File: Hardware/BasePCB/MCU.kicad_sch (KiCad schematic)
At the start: 24 parts, among them J7 Conn_01x04, Q10 IRLML0030, Q11 IRLML0030, U5 LeaderSOM

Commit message: only 4 traces left
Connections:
- net SuppReg_ADC: now also R9.1; no longer R40.1
- net SuppReg_ADC_filtered: now also C14.1, R9.2, U5.39 (ADC1_IN3); no longer C13.1, R40.2, U5.33 (ADC1_IN15)
- net SuppReg_I_ADC: now also R35.1; no longer R9.1
- net SuppReg_I_ADC_filtered: now also C11.1, R35.2, U5.31 (ADC1_IN12); no longer C14.1, R9.2, U5.39 (ADC1_IN3)
- net Supp_ADC: now also R45.1; no longer R35.1
- net Supp_ADC_filtered: now also C15.1, R45.2, U5.41 (ADC1_IN2); no longer C11.1, R35.2, U5.31 (ADC1_IN12)
- net Supp_I_ADC: now also R40.1; no longer R45.1
- net Supp_I_ADC_filtered: now also C13.1, R40.2, U5.33 (ADC1_IN15); no longer C15.1, R45.2, U5.41 (ADC1_IN2)
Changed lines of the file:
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@@
 	)
 	(junction
-		(at 52.07 104.14)
+		(at 121.92 72.39)
 		(diameter 0)
 		(color 0 0 0 0)
 	)
 	(junction
-		(at 121.92 72.39)
+		(at 121.92 74.93)
 		(diameter 0)
 		(color 0 0 0 0)
 	)
 	(junction
-		(at 107.95 104.14)
+		(at 34.29 26.67)
 		(diameter 0)
 		(color 0 0 0 0)
 	)
 	(junction
-		(at 121.92 74.93)
+		(at 121.92 64.77)
 		(diameter 0)
 		(color 0 0 0 0)
 	)
 	(junction
-		(at 34.29 26.67)
+		(at 107.95 128.27)
 		(diameter 0)
 		(color 0 0 0 0)
 	)
 	(junction
-		(at 121.92 64.77)
+		(at 52.07 129.54)
 		(diameter 0)
 		(color 0 0 0 0)
@@
 	)
 	(junction
-		(at 107.95 128.27)
+		(at 252.73 58.42)
 		(diameter 0)
 		(color 0 0 0 0)
 	)
 	(junction
-		(at 52.07 129.54)
+		(at 121.92 69.85)
 		(diameter 0)
 		(color 0 0 0 0)
 	)
 	(junction
-		(at 252.73 58.42)
+		(at 52.07 104.14)
 		(diameter 0)
 		(color 0 0 0 0)
 	)
 	(junction
-		(at 121.92 69.85)
+		(at 121.92 67.31)
 		(diameter 0)
 		(color 0 0 0 0)
 	)
 	(junction
-		(at 121.92 67.31)
+		(at 107.95 104.14)
 		(diameter 0)
 		(color 0 0 0 0)
@@
 	(wire
 		(pts
+			(xy 165.1 38.1) (xy 190.5 38.1)
+		)
+		(stroke
+			(width 0)
+			(type default)
+		)
+	)
+	(wire
+		(pts
 			(xy 252.73 30.48) (xy 255.27 30.48)
 		)
@@
 	(wire
 		(pts
+			(xy 39.37 129.54) (xy 41.91 129.54)
+		)
+		(stroke
+			(width 0)
+			(type default)
+		)
+	)
+	(wire
+		(pts
 			(xy 40.64 54.61) (xy 45.72 54.61)
 		)
@@
 	(wire
 		(pts
-			(xy 43.18 33.02) (xy 43.18 35.56)
+			(xy 52.07 129.54) (xy 73.66 129.54)
 		)
 		(stroke
@@
 	(wire
 		(pts
-			(xy 43.18 40.64) (xy 45.72 40.64)
+			(xy 43.18 33.02) (xy 43.18 35.56)
 		)
 		(stroke
@@
 	(wire
 		(pts
-			(xy 252.73 35.56) (xy 255.27 35.56)
+			(xy 43.18 40.64) (xy 45.72 40.64)
 		)
 		(stroke
@@
 	(wire
 		(pts
-			(xy 191.77 113.03) (xy 191.77 115.57)
+			(xy 252.73 35.56) (xy 255.27 35.56)
 		)
 		(stroke
@@
 	(wire
 		(pts
-			(xy 36.83 104.14) (xy 41.91 104.14)
+			(xy 191.77 113.03) (xy 191.77 115.57)
 		)
 		(stroke
@@
 	(wire
 		(pts
-			(xy 40.64 57.15) (xy 45.72 57.15)
+			(xy 52.07 104.14) (xy 74.93 104.14)
 		)
 		(stroke
@@
 	(wire
 		(pts
-			(xy 218.44 30.48) (xy 218.44 31.75)
+			(xy 40.64 57.15) (xy 45.72 57.15)
 		)
 		(stroke
@@
 	(wire
 		(pts
-			(xy 92.71 68.58) (xy 83.82 68.58)
+			(xy 218.44 30.48) (xy 218.44 31.75)
 		)
 		(stroke
@@
 	(wire
 		(pts
-			(xy 43.18 35.56) (xy 43.18 38.1)
+			(xy 92.71 68.58) (xy 83.82 68.58)
 		)
 		(stroke
@@
 	(wire
 		(pts
-			(xy 43.18 38.1) (xy 43.18 40.64)
+			(xy 43.18 35.56) (xy 43.18 38.1)
 		)
 		(stroke
@@
 	(wire
 		(pts
-			(xy 107.95 111.76) (xy 107.95 114.3)
+			(xy 43.18 38.1) (xy 43.18 40.64)
 		)
 		(stroke
@@
 	(wire
 		(pts
-			(xy 165.1 38.1) (xy 190.5 38.1)
+			(xy 107.95 111.76) (xy 107.95 114.3)
 		)
 		(stroke
@@
 	(wire
 		(pts
-			(xy 191.77 101.6) (xy 191.77 105.41)
+			(xy 107.95 104.14) (xy 130.81 104.14)
 		)
 		(stroke
@@
 	(wire
 		(pts
-			(xy 38.1 129.54) (xy 41.91 129.54)
+			(xy 191.77 101.6) (xy 191.77 105.41)
 		)
 		(stroke
@@
 	(wire
 		(pts
-			(xy 165.1 30.48) (xy 190.5 30.48)
+			(xy 83.82 53.34) (xy 96.52 53.34)
 		)
 		(stroke
@@
 	(wire
 		(pts
-			(xy 83.82 53.34) (xy 96.52 53.34)
+			(xy 191.77 115.57) (xy 195.58 115.57)
 		)
 		(stroke
@@
 	(wire
 		(pts
-			(xy 191.77 115.57) (xy 195.58 115.57)
+			(xy 93.98 104.14) (xy 97.79 104.14)
+		)
+		(stroke
+			(width 0)
+			(type default)
+		)
+	)
+	(wire
+		(pts
+			(xy 38.1 104.14) (xy 41.91 104.14)
 		)
 		(stroke
@@
 	(wire
 		(pts
-			(xy 118.11 38.1) (xy 127 38.1)
+			(xy 107.95 128.27) (xy 127 128.27)
 		)
 		(stroke
@@
 	(wire
 		(pts
-			(xy 107.95 104.14) (xy 127 104.14)
+			(xy 118.11 38.1) (xy 127 38.1)
 		)
 		(stroke
@@
 	(wire
 		(pts
-			(xy 52.07 129.54) (xy 74.93 129.54)
+			(xy 165.1 30.48) (xy 190.5 30.48)
 		)
 		(stroke
@@
 	(wire
 		(pts
+			(xy 93.98 128.27) (xy 97.79 128.27)
+		)
+		(stroke
+			(width 0)
+			(type default)
+		)
+	)
+	(wire
+		(pts
 			(xy 218.44 100.33) (xy 218.44 101.6)
 		)
@@
 	(wire
 		(pts
-			(xy 93.98 104.14) (xy 97.79 104.14)
+			(xy 165.1 71.12) (xy 186.69 71.12)
 		)
 		(stroke
@@
 	(wire
 		(pts
-			(xy 165.1 71.12) (xy 186.69 71.12)
+			(xy 242.57 69.85) (xy 259.08 69.85)
 		)
 		(stroke
@@
 	(wire
 		(pts
-			(xy 242.57 69.85) (xy 259.08 69.85)
+			(xy 165.1 33.02) (xy 190.5 33.02)
 		)
 		(stroke
@@
 	(wire
 		(pts
-			(xy 148.59 115.57) (xy 152.4 115.57)
+			(xy 165.1 43.18) (xy 190.5 43.18)
 		)
 		(stroke
@@
 	(wire
 		(pts
-			(xy 83.82 60.96) (xy 92.71 60.96)
+			(xy 148.59 115.57) (xy 152.4 115.57)
 		)
 		(stroke
@@
 	(wire
 		(pts
-			(xy 34.29 35.56) (xy 34.29 38.1)
+			(xy 83.82 60.96) (xy 92.71 60.96)
 		)
 		(stroke
@@
 	(wire
 		(pts
-			(xy 92.71 66.04) (xy 83.82 66.04)
+			(xy 34.29 35.56) (xy 34.29 38.1)
 		)
 		(stroke
@@
 	(wire
 		(pts
-			(xy 165.1 68.58) (xy 186.69 68.58)
+			(xy 92.71 66.04) (xy 83.82 66.04)
 		)
 		(stroke
@@
 	(wire
 		(pts
-			(xy 248.92 58.42) (xy 252.73 58.42)
+			(xy 165.1 68.58) (xy 186.69 68.58)
 		)
 		(stroke
@@
 	(wire
 		(pts
-			(xy 107.95 128.27) (xy 130.81 128.27)
+			(xy 248.92 58.42) (xy 252.73 58.42)
 		)
 		(stroke
@@
 	(wire
 		(pts
-			(xy 165.1 43.18) (xy 190.5 43.18)
-		)
-		(stroke
-			(width 0)
-			(type default)
-		)
-	)
-	(wire
-		(pts
-			(xy 93.98 128.27) (xy 97.79 128.27)
-		)
-		(stroke
-			(width 0)
-			(type default)
-		)
-	)
-	(wire
-		(pts
 			(xy 160.02 120.65) (xy 160.02 127)
 		)
@@
 		)
 	)
-	(wire
-		(pts
-			(xy 165.1 33.02) (xy 190.5 33.02)
-		)
-		(stroke
-			(width 0)
-			(type default)
-		)
-	)
 	(bus
 		(pts
@@
 	(wire
 		(pts
-			(xy 52.07 104.14) (xy 71.12 104.14)
-		)
-		(stroke
-			(width 0)
-			(type default)
-		)
-	)
-	(wire
-		(pts
 			(xy 52.07 111.76) (xy 52.07 114.3)
 		)
@@
 	)
 	(label "SuppReg_ADC_filtered"
-		(at 127 104.14 180)
+		(at 73.66 129.54 180)
 		(effects
 			(font
@@
 	)
 	(label "Supp_I_ADC_filtered"
-		(at 130.81 128.27 180)
+		(at 130.81 104.14 180)
 		(effects
 			(font
@@
 	)
 	(label "Supp_ADC_filtered"
-		(at 71.12 104.14 180)
+		(at 127 128.27 180)
 		(effects
 			(font
@@
 	)
 	(label "SuppReg_ADC_filtered"
-		(at 190.5 33.02 180)
+		(at 190.5 38.1 180)
 		(effects
 			(font
@@
 	)
 	(label "Supp_ADC_filtered"
-		(at 190.5 30.48 180)
+		(at 190.5 43.18 180)
 		(effects
 			(font
@@
 	)
 	(label "SuppReg_I_ADC_filtered"
-		(at 74.93 129.54 180)
+		(at 74.93 104.14 180)
 		(effects
 			(font
@@
 	)
 	(label "SuppReg_I_ADC_filtered"
-		(at 190.5 38.1 180)
+		(at 190.5 30.48 180)
 		(effects
 			(font
@@
 	)
 	(label "Supp_I_ADC_filtered"
-		(at 190.5 43.18 180)
+		(at 190.5 33.02 180)
 		(effects
 			(font
@@
 	(hierarchical_label "SuppReg_ADC"
 		(shape input)
-		(at 93.98 104.14 180)
+		(at 39.37 129.54 180)
 		(effects
 			(font
@@
 	(hierarchical_label "SuppReg_I_ADC"
 		(shape input)
-		(at 38.1 129.54 180)
+		(at 38.1 104.14 180)
 		(effects
 			(font
@@
 	(hierarchical_label "Supp_I_ADC"
 		(shape input)
-		(at 93.98 128.27 180)
+		(at 93.98 104.14 180)
 		(effects
 			(font
@@
 	(hierarchical_label "Supp_ADC"
 		(shape input)
-		(at 36.83 104.14 180)
+		(at 93.98 128.27 180)
 		(effects
 			(font

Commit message: align things
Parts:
- added D6: LED, LED_SMD:LED_0603_1608Metric_Pad1.05x0.95mm_HandSolder, symbol Device:LED
- added R12: 120, Resistor_SMD:R_0603_1608Metric_Pad0.98x0.95mm_HandSolder, symbol Device:R
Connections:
- net GND: now also D6.1 (K)
- net Heartbeat: now reaches U5.36 (UART4_RX)
- net Heartbeat: now also R12.1
- new net: D6.2 (A), R12.2
- no-connect marks 7 -> 6
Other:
- moved on the sheet: J7, R7, R8

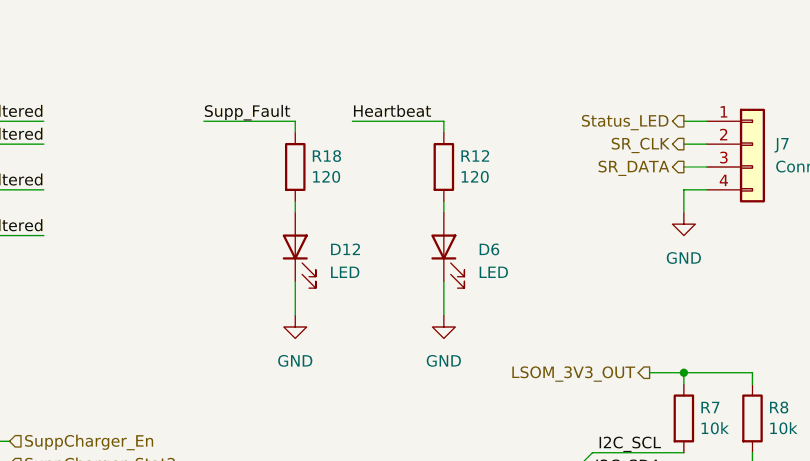
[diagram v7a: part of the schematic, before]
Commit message: add JLC p/n
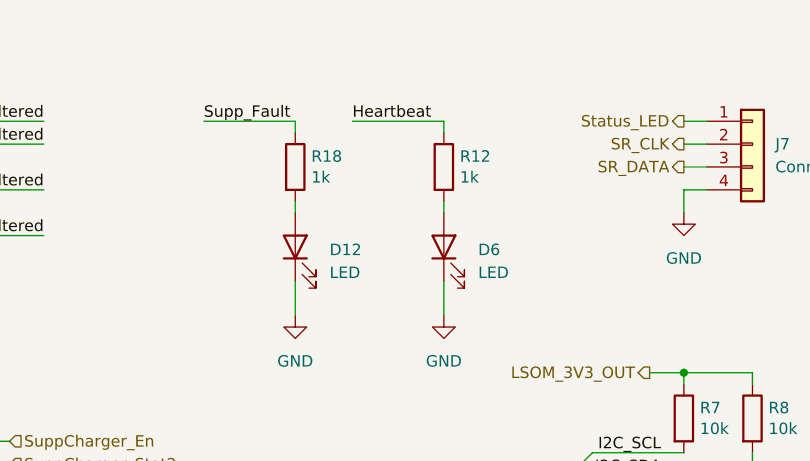
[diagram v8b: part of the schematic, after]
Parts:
- C11, C13, C14, C15: Assemble (none) -> Y; LSCC P/N (none) -> C1622
- D10, D12, D6: Assemble (none) -> Y; LSCC P/N (none) -> C7371904
- J7, U5: Assemble (none) -> N
- Q10, Q11: Assemble (none) -> Y; LSCC P/N (none) -> C67272; P/N (none) -> IRLML0030
- R10, R11, R21, R22, R23, R24, R7, R8: Assemble (none) -> Y; LSCC P/N (none) -> C25804
- R12, R18: value 120 -> 1k; Assemble (none) -> Y; LSCC P/N (none) -> C21190; P/N CRCW0603120RFKEC -> CRCW06031K00FKEI
- R26, R35, R40, R45, R9: Assemble (none) -> Y; LSCC P/N (none) -> C23162
